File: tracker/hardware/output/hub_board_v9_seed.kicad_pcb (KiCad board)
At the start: 4 copper layers, 103 x 103 mm, 39 parts, among them U1 ESP32-S3-WROOM-1U-N8R8, U2 LoRa2021F33-2G4, U3 LoRa2021_Castellated, U4 SX1280, U5 MAX-M10S, U6 MS5611-01BA, U7 TPS7A02

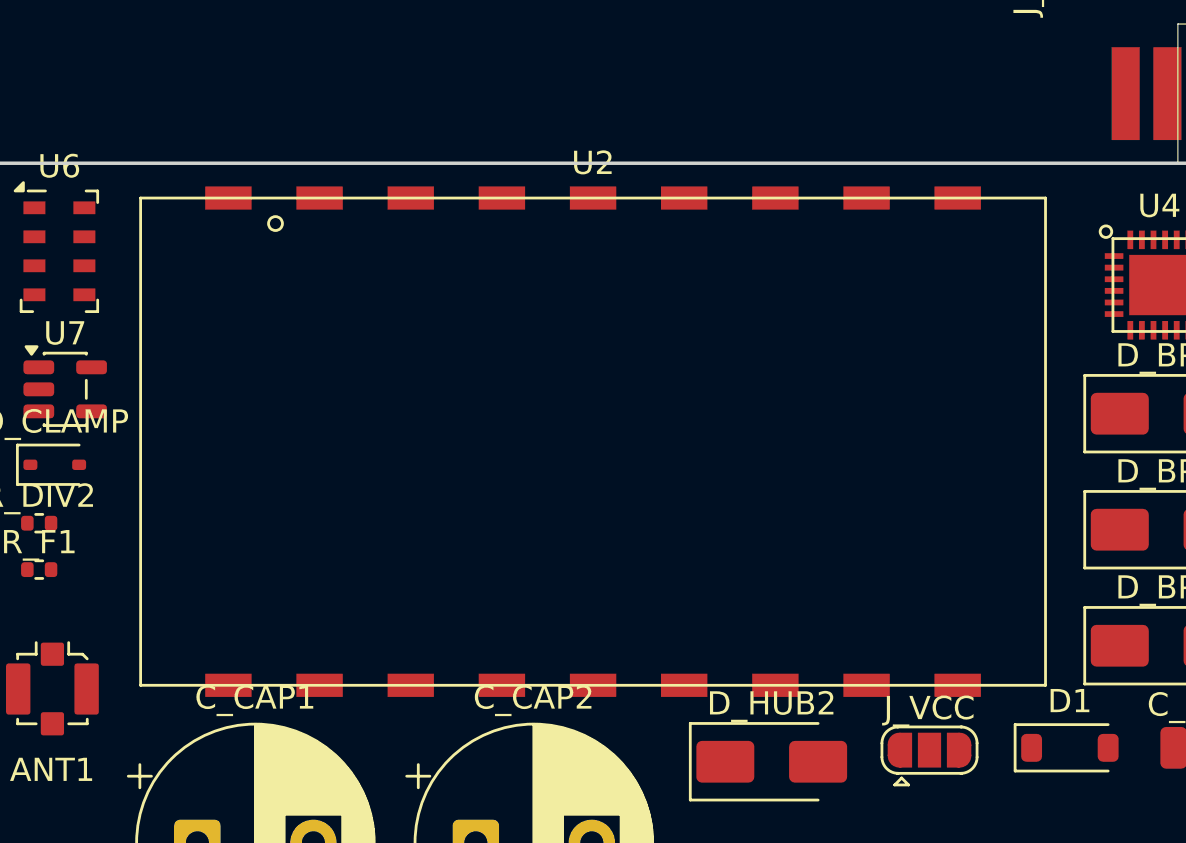
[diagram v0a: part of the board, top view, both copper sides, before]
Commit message: fix(hw/f33): derive the castellation land size from the operator-supplied 0.80mm datum
The F33 land pattern's pad POSITIONS were already verified against the vendor's own
Altium pad file; the pad SIZE was the one declared guess (2.0 x 1.0 mm, TODO(unverified)).
The operator read the vendor drawing (datasheet s9 "Mechanism Dimension" p8, an embedded
JPEG raster with no text layer, hence never extractable in-repo) and reported the
castellation hole diameter D = 0.80 +/- 0.10 mm.  That is the authoritative datum.

DERIVE the land instead of hard-coding it:
  rule: land = the castellation aperture grown by a uniform 0.25mm solder-fillet margin
        on every side.
    x (along the edge): D + 2*0.25 = 1.30mm  (was 2.0mm = 2.5xD);
                        gap to the next land = 3.9289 - 1.30 = 2.6289mm
    y (across the edge): D + 2*0.25 = 1.30mm, symmetric about the pad centre, which the
                        vendor file pins on the module edge and which must NOT move:
                          inward 0.65mm >= D/2 = 0.40mm
                          outward 0.65mm >= inward 0.65mm -- the hand-solder iron's
                          access is the design driver (every joint on this vehicle is
                          hand-soldered); 0.65mm clears a 0.5mm chisel tip.

- scripts/gen_f33_landpattern.py: the hard-coded LAND_*_MM constants are replaced by the
  derivation (CASTELLATION_D_MM, CASTELLATION_D_TOL_MM, LAND_FILLET_MARGIN_MM); the rule
  and arithmetic are in the docstring; the datum and its +/-0.1 tolerance are recorded;
  --land-length/--land-width are kept as explicit overrides; the TODO(unverified)
  land-size flag is DROPPED (no other TODO touched).
- All four committed footprint copies and the v9 design-of-record footprint regenerated.
  Pad POSITIONS unchanged: the 18 pad-centre list is byte-identical (sha256 960877b2...)
  before and after, the bbox is still 31.4312 x 21.0000mm, and only the pad-size histogram
  moves 2x1 -> 1.3x1.3.  --verify-all exits 0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
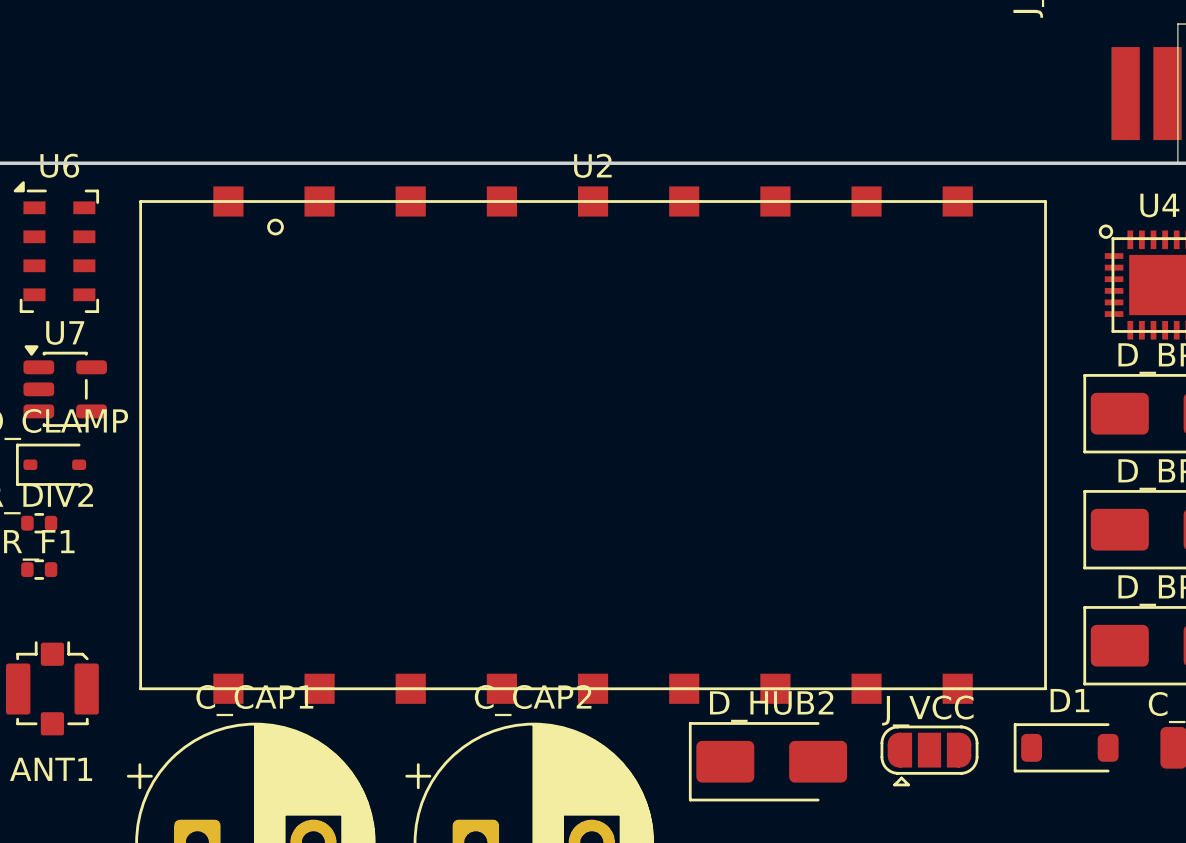
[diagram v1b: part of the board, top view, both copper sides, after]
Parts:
- moved U2 0.15 mm to (25.8, 12.2)
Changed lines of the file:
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@@
 	(footprint "balloon_flight_v9:LoRa2021F33_2G4"
 		(layer "F.Cu")
-		(at 25.845 12)
-		(descr "NiceRF LoRa2021F33-2G4, 18-pin castellated module (LR2021 + 2W PA + TCXO), 39x21mm. Pad CENTRES decoded from the vendor land file LORA2021F33-2G4 footprint_pads.pcb (pitch 3.9289mm, 9 pads on each 39mm edge). Land size 2.0x1.0 mm TODO(unverified): datasheet s9 p8 is a raster with no text layer.")
+		(at 25.845 12.15)
+		(descr "NiceRF LoRa2021F33-2G4, 18-pin castellated module (LR2021 + 2W PA + TCXO), 39x21mm. Pad CENTRES decoded from the vendor land file LORA2021F33-2G4 footprint_pads.pcb (pitch 3.9289mm, 9 pads on each 39mm edge). Land size 1.3 x 1.3 mm DERIVED from the operator-supplied castellation hole diameter D = 0.8 +/- 0.1 mm grown by a uniform 0.25 mm solder-fillet margin on every side (datasheet s9 p8, read by the operator 2026-10-07).")
 		(tags "LoRa LR2021 NiceRF F33 castellated PA 2W vendor-land-pattern")
 		(property "Reference" "U2"
@@
 		(pad "1" smd rect
 			(at -11.7867 -10.5)
-			(size 2 1)
+			(size 1.3 1.3)
 			(layers "F.Cu" "F.Mask" "F.Paste")
 			(net 17 "/F33_VCC")
@@
 		(pad "2" smd rect
 			(at -7.8578 -10.5)
-			(size 2 1)
+			(size 1.3 1.3)
 			(layers "F.Cu" "F.Mask" "F.Paste")
 			(net 51 "GND")
@@
 		(pad "3" smd rect
 			(at -3.9289 -10.5)
-			(size 2 1)
+			(size 1.3 1.3)
 			(layers "F.Cu" "F.Mask" "F.Paste")
 			(net 51 "GND")
@@
 		(pad "4" smd rect
 			(at 0 -10.5)
-			(size 2 1)
+			(size 1.3 1.3)
 			(layers "F.Cu" "F.Mask" "F.Paste")
 			(net 51 "GND")
@@
 		(pad "5" smd rect
 			(at 3.9289 -10.5)
-			(size 2 1)
+			(size 1.3 1.3)
 			(layers "F.Cu" "F.Mask" "F.Paste")
 			(net 1 "+3V3")
@@
 		(pad "6" smd rect
 			(at 7.8578 -10.5)
-			(size 2 1)
+			(size 1.3 1.3)
 			(layers "F.Cu" "F.Mask" "F.Paste")
 			(net 51 "GND")
@@
 		(pad "7" smd rect
 			(at 11.7867 -10.5)
-			(size 2 1)
+			(size 1.3 1.3)
 			(layers "F.Cu" "F.Mask" "F.Paste")
 			(net 51 "GND")
@@
 		(pad "8" smd rect
 			(at 15.7156 -10.5)
-			(size 2 1)
+			(size 1.3 1.3)
 			(layers "F.Cu" "F.Mask" "F.Paste")
 			(net 51 "GND")
@@
 		(pad "9" smd rect
 			(at 15.7156 10.5)
-			(size 2 1)
+			(size 1.3 1.3)
 			(layers "F.Cu" "F.Mask" "F.Paste")
 			(net 2 "/ANT1_433_TX")
@@
 		(pad "10" smd rect
 			(at 11.7867 10.5)
-			(size 2 1)
+			(size 1.3 1.3)
 			(layers "F.Cu" "F.Mask" "F.Paste")
 		)
 		(pad "11" smd rect
 			(at 7.8578 10.5)
-			(size 2 1)
+			(size 1.3 1.3)
 			(layers "F.Cu" "F.Mask" "F.Paste")
 			(net 51 "GND")
@@
 		(pad "12" smd rect
 			(at 3.9289 10.5)
-			(size 2 1)
+			(size 1.3 1.3)
 			(layers "F.Cu" "F.Mask" "F.Paste")
 			(net 16 "/F33_SCK")
@@
 		(pad "13" smd rect
 			(at 0 10.5)
-			(size 2 1)
+			(size 1.3 1.3)
 			(layers "F.Cu" "F.Mask" "F.Paste")
 			(net 11 "/F33_CS_N")
@@
 		(pad "14" smd rect
 			(at -3.9289 10.5)
-			(size 2 1)
+			(size 1.3 1.3)
 			(layers "F.Cu" "F.Mask" "F.Paste")
 			(net 10 "/F33_BUSY")
@@
 		(pad "15" smd rect
 			(at -7.8578 10.5)
-			(size 2 1)
+			(size 1.3 1.3)
 			(layers "F.Cu" "F.Mask" "F.Paste")
 			(net 14 "/F33_MOSI")
@@
 		(pad "16" smd rect
 			(at -11.7867 10.5)
-			(size 2 1)
+			(size 1.3 1.3)
 			(layers "F.Cu" "F.Mask" "F.Paste")
 			(net 13 "/F33_MISO")
@@
 		(pad "17" smd rect
 			(at -15.7156 10.5)
-			(size 2 1)
+			(size 1.3 1.3)
 			(layers "F.Cu" "F.Mask" "F.Paste")
 			(net 15 "/F33_RESET_N")
@@
 		(pad "18" smd rect
 			(at -15.7156 -10.5)
-			(size 2 1)
+			(size 1.3 1.3)
 			(layers "F.Cu" "F.Mask" "F.Paste")
 			(net 12 "/F33_IRQ")

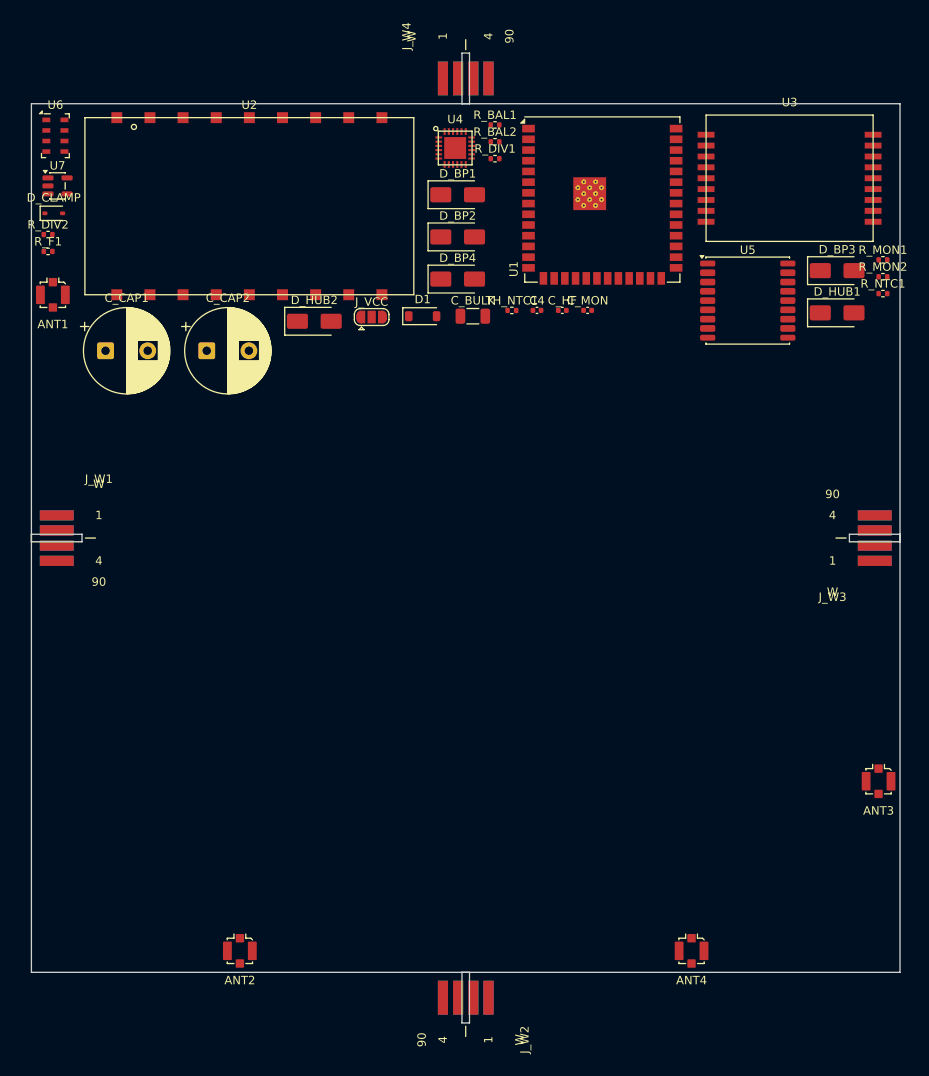
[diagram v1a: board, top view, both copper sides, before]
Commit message: fix(hub): STALE published board -- build's KRT_DIR was a path that does not exist; publish now REFUSES instead of silently no-oping
CLOSES THE OUTLINE FAIL IN MY OWN GATE, AND THE ROOT CAUSE WAS A REAL DEFECT, NOT A STALE FILE.

=== THE MEASURED DIAGNOSIS ===
The two hub boards disagreed on the outline:
    tracker/hardware/hub_board_v9.kicad_pcb (committed): Edge.Cuts 103.150 x 103.150 mm, 0 tracks
    docs/fab/hub-v9/gerbers/hub_v9.kicad_pcb (packaged): Edge.Cuts  70.150 x 70.150 mm, 537 tracks
Both carry the SAME 39 footprints. ADR-068 (revised 2026-10-14) sets the outline at 70 x 70, and
build_hub_board_v9.py is the SINGLE WRITER of the committed file with DEFAULT_W/H = 70.0. So the
committed file was STALE at the SUPERSEDED ADR-055 D5 103x103-class outline.

I ALSO CORRECTED MY OWN GATE, WHICH WAS WRONG: the check compared GetBoardEdgesBoundingBox(), which is
inflated by TRACK/VIA/COPPER extents, not just the outline. That is why it reported the packaged board
as 70.15 x 71.65 -- the extra 1.50 mm of height was COPPER reaching past the edge, NOT the board being
taller. A FALSE divergence FAIL against a board that was fine. The check now measures Edge.Cuts DRAWING
ITEMS ONLY, and reports 70.15 x 70.15 for both. (Both boards also carry a uniform 0.075 mm outset on
every side -- 103.075 - (-0.075) = 103.150 -- a drawing convention, so outline-to-outline is the
correct comparison, never nominal-against-measured.)

=== THE ROOT CAUSE: A PATH THAT DOES NOT EXIST, AND A RETURN CODE NOBODY CHECKED ===
KRT_DIR was hard-coded to ~/tools/KiCadRoutingTools, WHICH DOES NOT EXIST ON THIS HOST -- the real
checkout is ~/repos/KiCadRoutingTools -> /data/repos/KiCadRoutingTools. run_krt therefore took its
"placer absent" branch, printed a note, and returned 1 -- AND main() DISCARDED THE RETURN CODE, so
--publish reported success while leaving the STALE committed board in place. That is exactly how the
103.15 x 103.15 outline survived: the publish never happened and nothing said 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
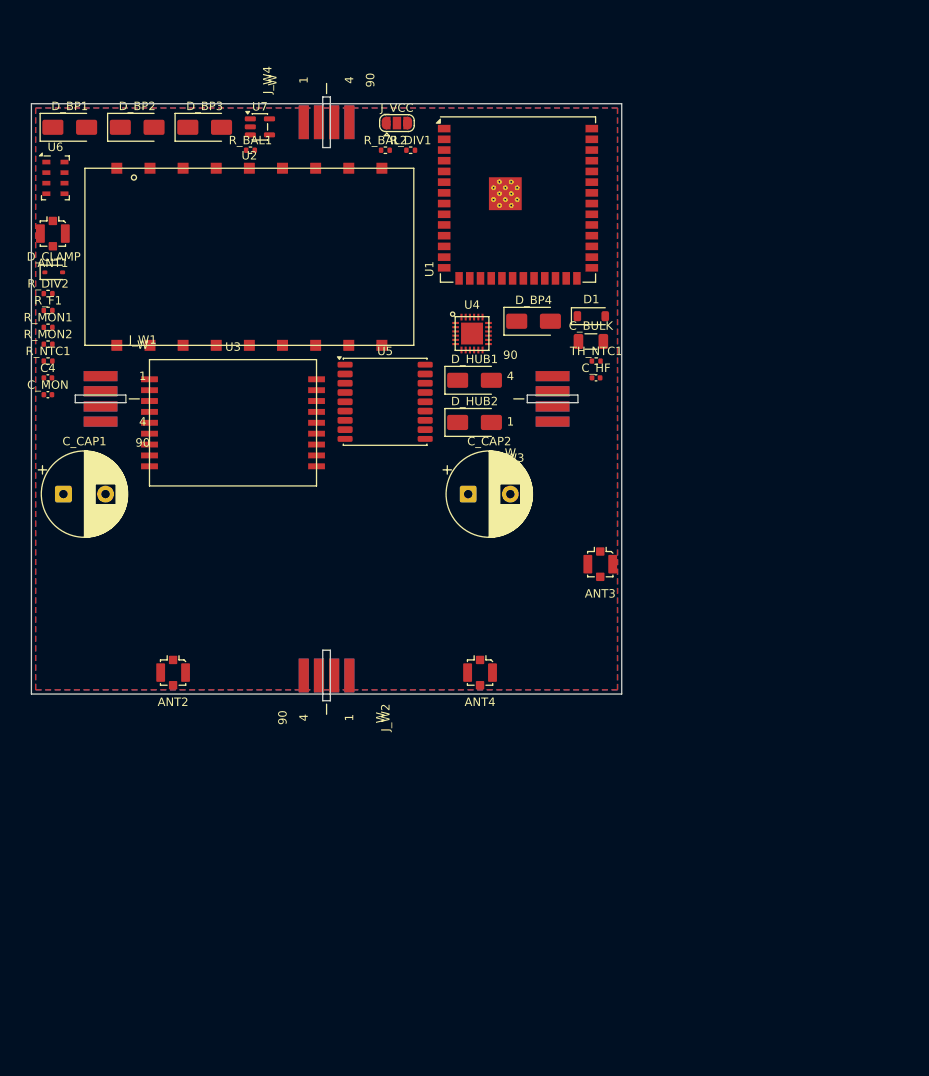
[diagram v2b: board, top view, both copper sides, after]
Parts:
- moved R_MON1 99.3 mm to (1.98, 26.5)
- moved R_MON2 99.3 mm to (1.98, 28.5)
- moved R_NTC1 99.3 mm to (1.98, 30.5)
- moved D_BP3 76.9 mm to (20.5, 2.79)
- moved U3 72.1 mm to (23.9, 37.8)
- moved C_MON 64.8 mm to (1.96, 34.5)
- moved C4 58.5 mm to (1.96, 32.5)
- moved D_BP1 46.7 mm to (4.54, 2.79)
- moved U5 44.6 mm to (41.9, 35.3)
- moved D_HUB1 43.7 mm to (52.5, 32.8)
- moved ANT3 41.9 mm to (67.5, 54.6)
- moved J_W2 41.6 mm to (35.0, 64.8)
- moved J_W3 41.6 mm to (64.8, 35.0)
- moved ANT4 41.4 mm to (53.2, 67.5)
- moved D_BP2 40.2 mm to (12.5, 2.79)
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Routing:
- added copper zone on B.Cu, net GND
- added copper zone on F.Cu, net GND
- added copper zone on In1.Cu, net GND
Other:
- board size 103 x 103 mm -> 70 x 70 mm
